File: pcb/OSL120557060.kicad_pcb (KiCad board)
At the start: 2 copper layers, 115.6 x 108 mm, 87 parts, among them J1 USB_C_Plug_USB2.0, J2 USB_C_Plug_USB2.0, J3 AVR-ISP-6, SW1 SW_SPST, SW10 SW_SPST, SW11 SW_SPST, SW12 SW_SPST, SW13 SW_SPST, SW14 SW_SPST, SW15 SW_SPST, SW16 SW_SPST, SW17 SW_SPST, SW18 SW_SPST, SW19 SW_SPST, SW2 SW_SPST, SW20 SW_SPST, SW21 SW_SPST, SW22 SW_SPST, SW23 SW_SPST, SW24 SW_SPST, SW25 SW_SPST, SW26 SW_SPST, SW27 SW_SPST, SW28 SW_SPST, SW29 SW_SPST, SW3 SW_SPST, SW30 SW_SPST, SW4 SW_SPST, SW5 SW_SPST, SW6 SW_SPST, SW7 SW_SPST, SW8 SW_SPST, SW9 SW_SPST, U1 ATmega328-PU, X1 16MHz

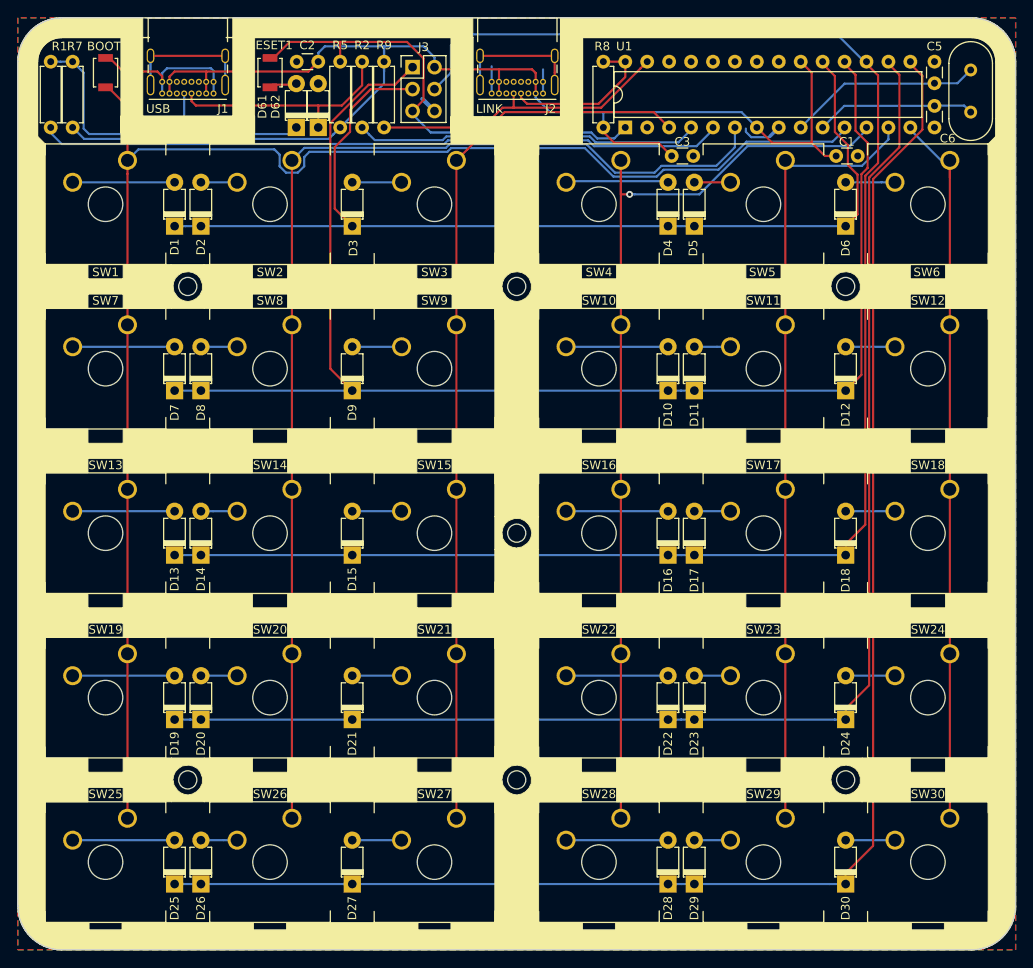
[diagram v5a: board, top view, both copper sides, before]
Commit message: * added pulldown resistors to allow usb-c usb-c cables * fixed usb-c footprint for reversibility
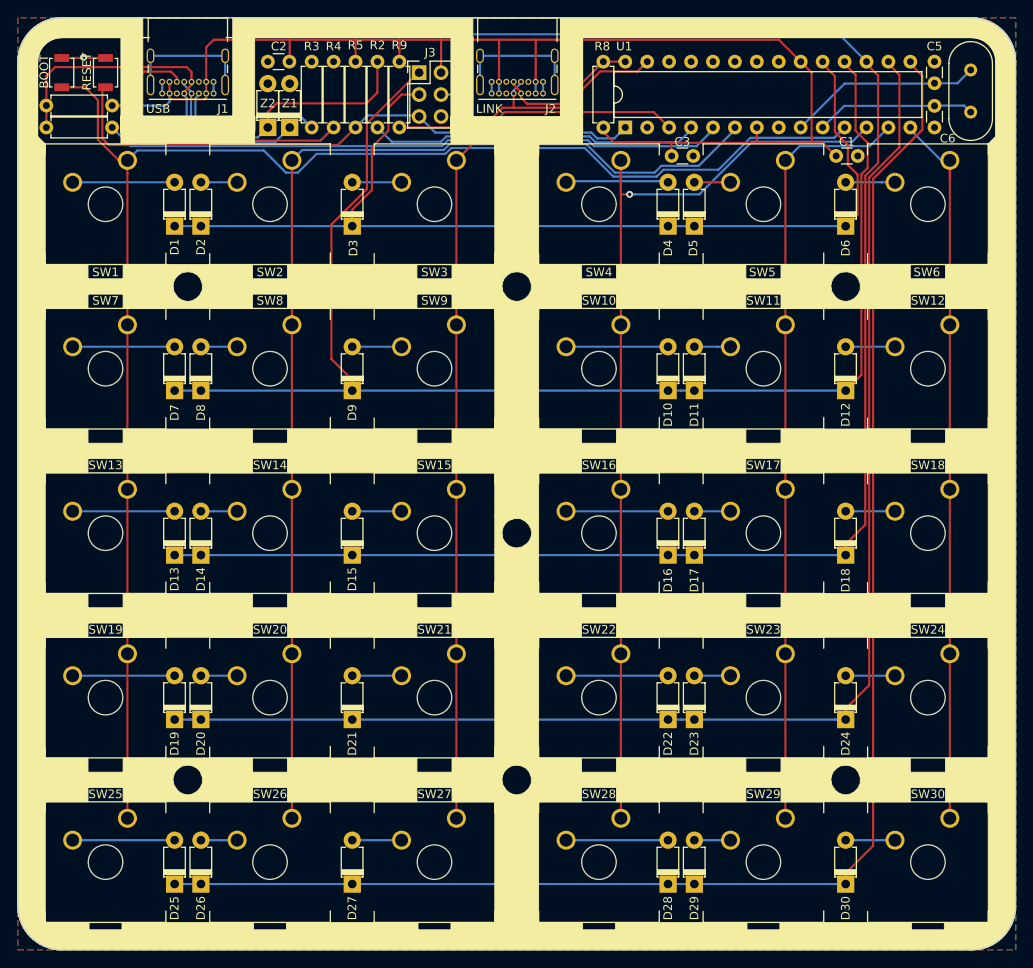
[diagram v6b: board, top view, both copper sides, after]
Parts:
- removed REF** (x7): MountingHole_2.1mm, MountingHole:MountingHole_2.1mm
- added R3: 5k1, Resistor_THT:R_Axial_DIN0207_L6.3mm_D2.5mm_P7.62mm_Horizontal, F.Cu at (82.3, 61.0)
- added R4: 5k1, Resistor_THT:R_Axial_DIN0207_L6.3mm_D2.5mm_P7.62mm_Horizontal, F.Cu at (84.8, 61.0)
- moved RESET 19.0 mm to (58.4, 54.6), turned to 270 degrees
- moved R5 7.82 mm to (87.4, 53.3), turned to 270 degrees
- moved R1 7.64 mm to (51.6, 61.0), turned to 0 degrees
- moved R7 5.92 mm to (51.6, 58.4), turned to 0 degrees
- moved Z2 5.84 mm to (77.2, 61.0)
- moved BOOT 5.08 mm to (53.3, 54.6)
- moved C2 3.34 mm to (79.7, 53.3)
- moved R9 1.78 mm to (92.5, 61.0)
- moved R2 1.78 mm to (89.9, 61.0)
- moved J3 0.99 mm to (94.7, 54.6)
- moved Z1 0.76 mm to (79.8, 61.0)
- renumbered BOOT1 to BOOT, RESET1 to RESET, D62 to Z1, D61 to Z2
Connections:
- J1 pad A5: (no net) -> Net-(J1-PadA5)
- J1 pad B5: (no net) -> Net-(J1-PadB5)
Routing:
- net Net-(J1-PadB5): track 0.00 -> 35.8 mm
- net GND: track 36.9 -> 10.5 mm, vias 0 -> 1
- net Net-(J1-PadA5): track 0.00 -> 19.9 mm
- net /Reset: track 55.2 -> 70.8 mm
- net Net-(J1-PadA6): track 27.1 -> 34.6 mm
- net /USB_D-: track 78.5 -> 71.8 mm
- net +5V: track 161.8 -> 157.7 mm
- net /Row1: track 122.4 -> 118.8 mm
- net Net-(J1-PadA7): track 40.5 -> 43.9 mm
- net /Col1: track 176.8 -> 179.5 mm
- net /SCL: track 18.5 -> 16.6 mm
- net /Row2: track 162.0 -> 160.1 mm
- net /USB_D+: track 39.8 -> 38.2 mm
- net /Col2: track 132.9 -> 131.7 mm
- net /Col5: track 90.8 -> 89.7 mm
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
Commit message: silkscreen updates
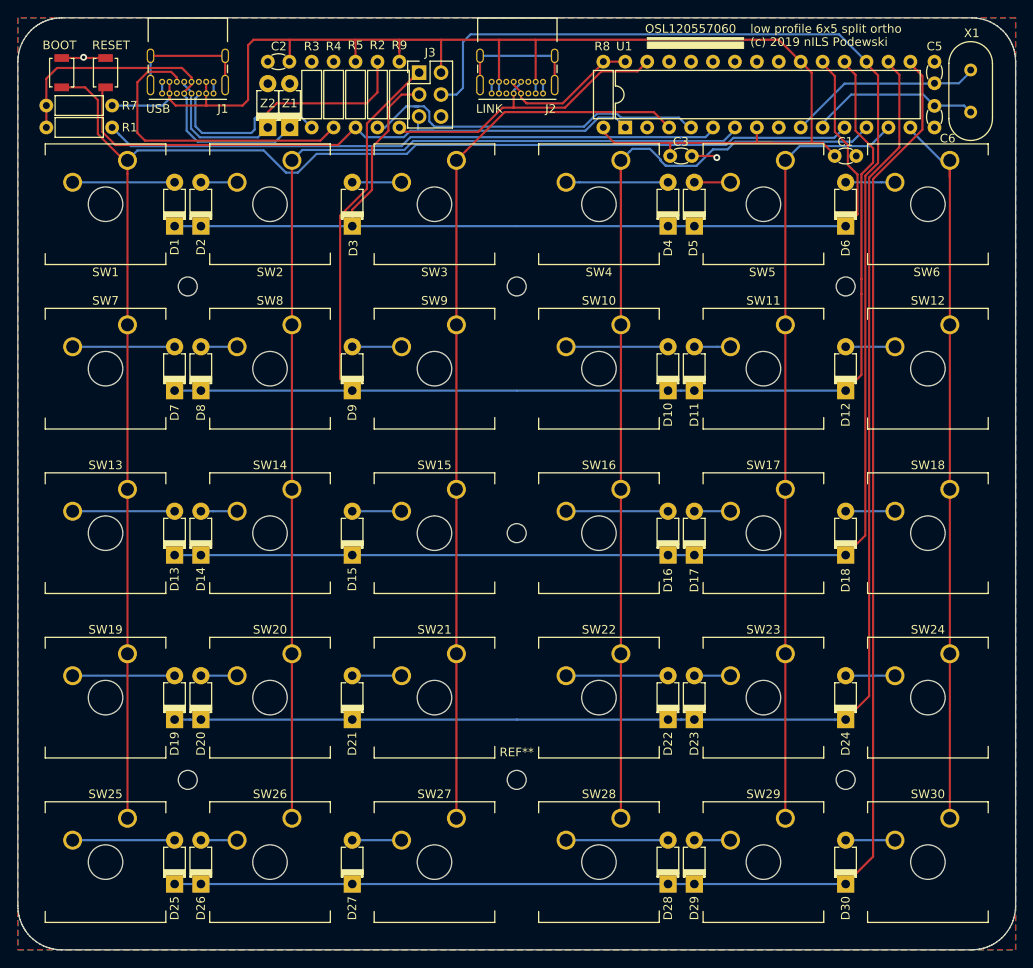
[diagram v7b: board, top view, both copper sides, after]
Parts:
- added REF**: MountingHole_2.2mm_M2, MountingHole:MountingHole_2.2mm_M2, F.Cu at (144.1, 136.5)
- added REF**: MountingHole_2.2mm_M2, MountingHole:MountingHole_2.2mm_M2, F.Cu at (144.1, 79.4)
- added REF**: MountingHole_2.2mm_M2, MountingHole:MountingHole_2.2mm_M2, F.Cu at (106.0, 79.4)
- added REF**: MountingHole_2.2mm_M2, MountingHole:MountingHole_2.2mm_M2, F.Cu at (106.0, 108.0)
- added REF**: MountingHole_2.2mm_M2, MountingHole:MountingHole_2.2mm_M2, F.Cu at (106.0, 136.5)
- added REF**: MountingHole_2.2mm_M2, MountingHole:MountingHole_2.2mm_M2, F.Cu at (67.9, 136.5)
- added REF**: MountingHole_2.2mm_M2, MountingHole:MountingHole_2.2mm_M2, F.Cu at (67.9, 79.4)
- moved C1 0.17 mm to (142.9, 64.3)
- moved C3 0.17 mm to (123.8, 64.3)
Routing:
- net +5V: track 157.7 -> 161.2 mm
- net /Col1: track 179.5 -> 176.4 mm
- net GND: track 10.5 -> 13.4 mm, vias 1 -> 2
- net /Col2: track 131.7 -> 129.0 mm
- net /USB_D+: track 38.2 -> 40.8 mm
- net /Reset: track 70.8 -> 73.2 mm
- net /Xtal_P: track 18.8 -> 20.1 mm
- net /USB_D-: track 71.8 -> 71.3 mm
- net Net-(J1-PadA7): track 43.9 -> 43.3 mm
- net /Col4: track 111.8 -> 111.9 mm, vias 1 -> 0
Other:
- board text added: "(c) 2019 nILS Podewski"
- board text added: "OSL120557060"
- board text added: "low profile 6x5 split ortho"

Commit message: - added first revision BOM - improved base layout for plates
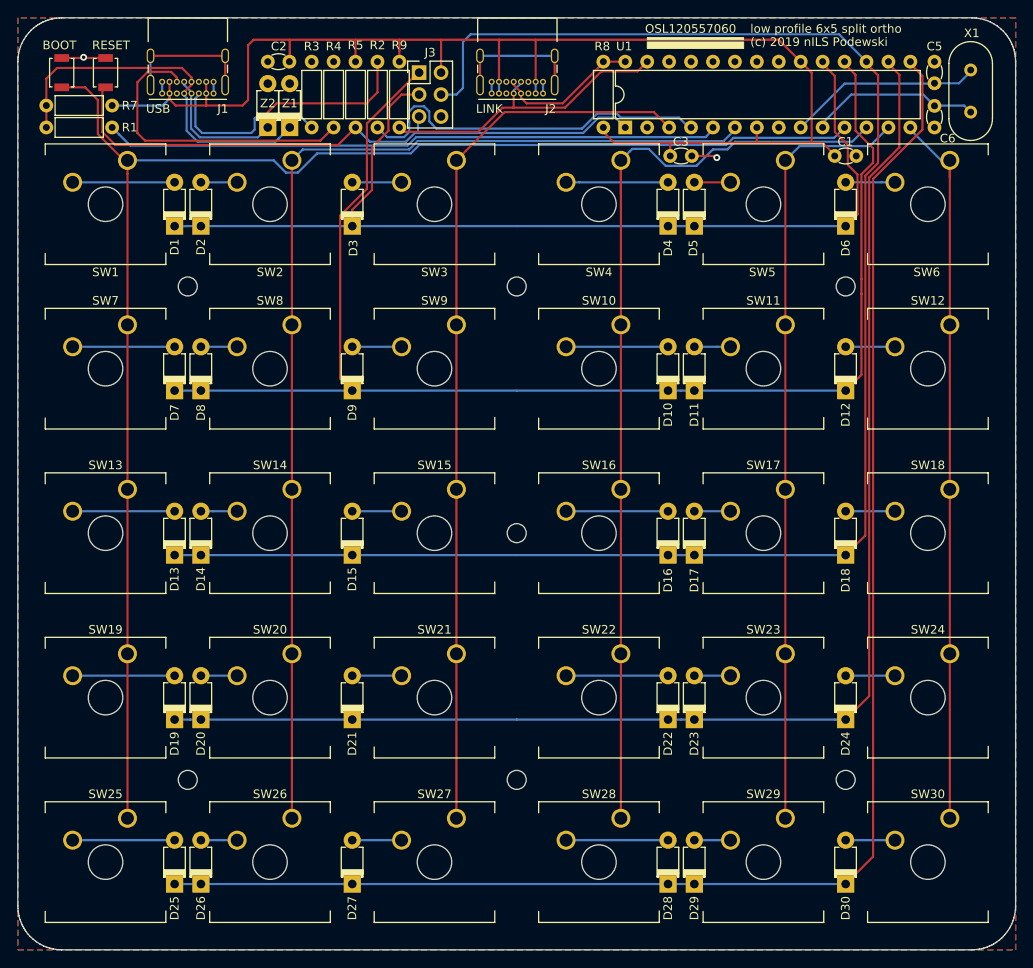
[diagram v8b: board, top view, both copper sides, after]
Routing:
- net /USB_D+: track 40.8 -> 42.9 mm
- net /Reset: track 73.2 -> 72.1 mm
- net /Col1: track 176.4 -> 175.4 mm
